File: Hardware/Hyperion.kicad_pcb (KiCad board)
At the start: 2 copper layers, 90.2 x 95.9 mm, 1 part

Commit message: Rough USB interface
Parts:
- added D1: TVS, CAPC1005-N, F.Cu at (182.0, 126.5)
- added D2: TVS, CAPC1005-N, F.Cu at (182.0, 124.2)
- added J1: CONN-DC, CONN-DC-CUI-202, F.Cu at (191.0, 112.0)
- added J2: USB, CONN-USB-MICRO-B-FCI, F.Cu at (190.0, 125.0)
- added R1: MOV, RESC1005-N, F.Cu at (184.0, 127.0)
- added R2: MOV, RESC1005-N, F.Cu at (184.0, 123.0)
- added TH1: PTC, RESC1005-N, F.Cu at (183.0, 129.5)
- added U1: FT2232H, QFP50P1200X1200-64N, F.Cu at (169.8, 124.8)
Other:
- net class Default: clearance 0.254 -> 0.2032; trace_width 0.254 -> 0.2032
- rule trace_clearance: 0.254 -> 0.2032
- rule trace_min: 0.254 -> 0.1524

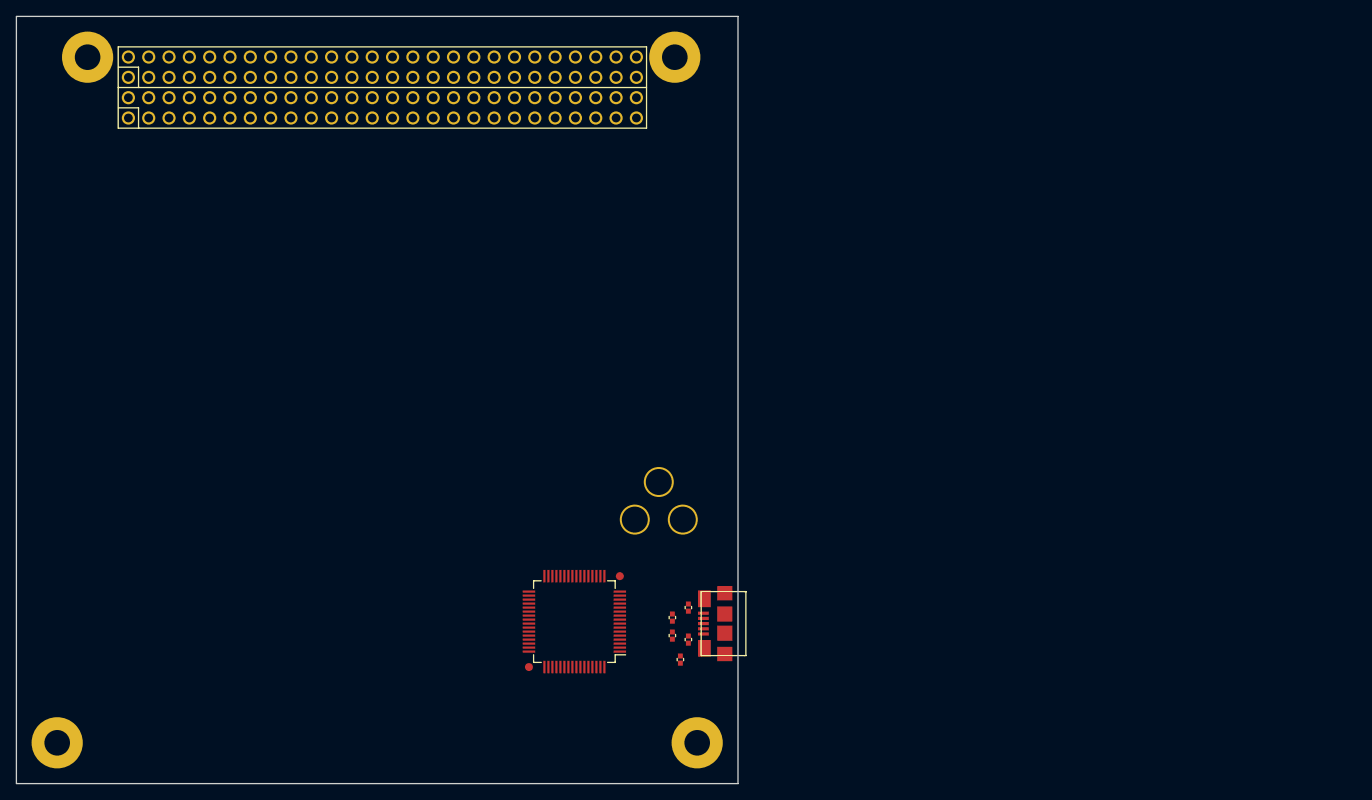
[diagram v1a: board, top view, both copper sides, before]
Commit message: Add protection circuit to DC jack
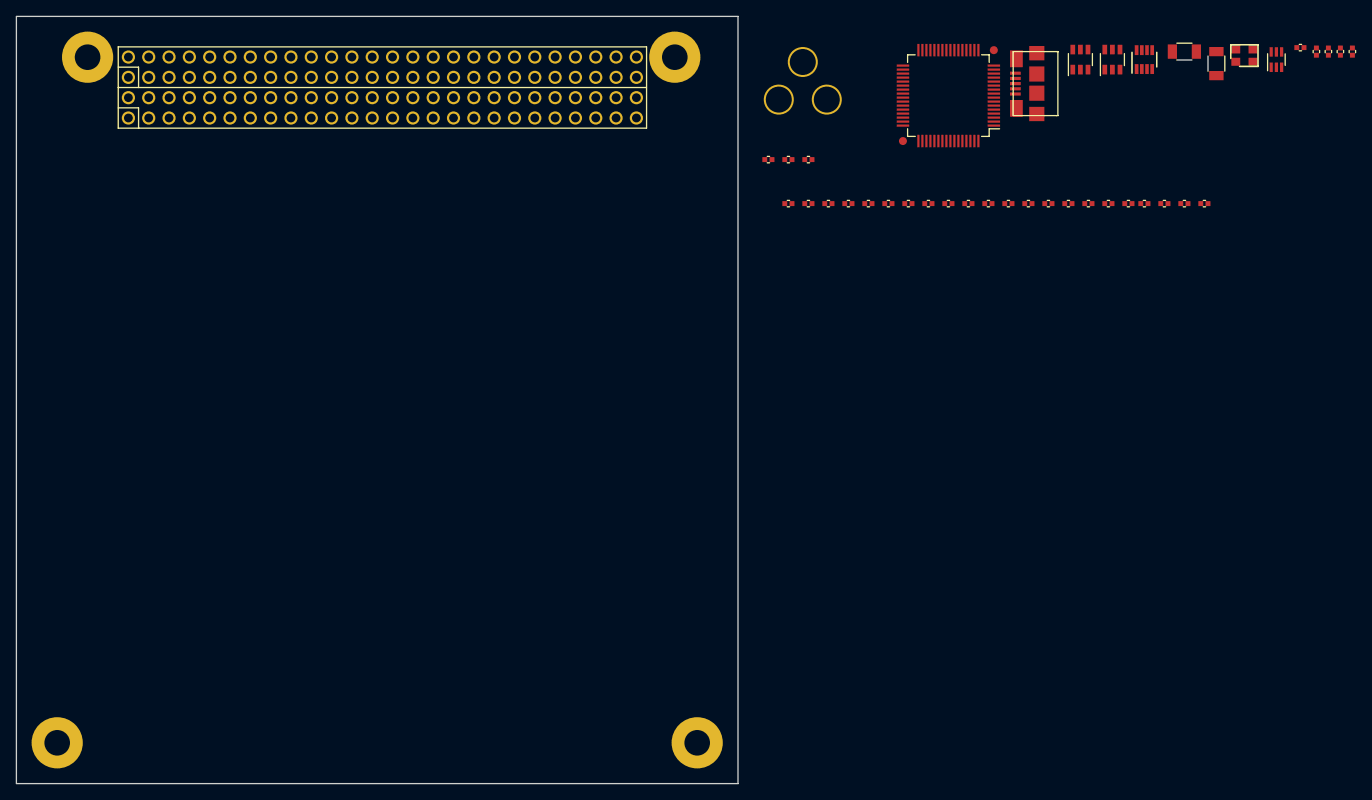
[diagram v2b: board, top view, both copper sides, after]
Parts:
- added C1: 3.3uF, CAPC1005-N, F.Cu at (229.0, 72.5)
- added C10: 0.1uF, CAPC1005-N, F.Cu at (199.0, 72.5)
- added C11: 27pF, CAPC1005-N, F.Cu at (234.0, 72.5)
- added C12: 0.1uF, CAPC1005-N, F.Cu at (216.5, 72.5)
- added C13: 0.1uF, CAPC1005-N, F.Cu at (236.5, 72.5)
- added C14: 27pF, CAPC1005-N, F.Cu at (231.5, 72.5)
- added C15: 0.1uF, CAPC1005-N, F.Cu at (224.0, 72.5)
- added C16: 0.1uF, CAPC1005-N, F.Cu at (260.5, 53.0)
- added C2: 0.1uF, CAPC1005-N, F.Cu at (214.0, 72.5)
- added C3: 3.3uF, CAPC1005-N, F.Cu at (226.5, 72.5)
- added C4: 0.1uF, CAPC1005-N, F.Cu at (211.5, 72.5)
- added C5: 0.1uF, CAPC1005-N, F.Cu at (209.0, 72.5)
- added C6: 3.3uF, CAPC1005-N, F.Cu at (221.5, 72.5)
- added C7: 0.1uF, CAPC1005-N, F.Cu at (206.5, 72.5)
- added C8: 0.1uF, CAPC1005-N, F.Cu at (204.0, 72.5)
- added C9: 0.1uF, CAPC1005-N, F.Cu at (201.5, 72.5)
- added FB1: 600, INDC1005-N, F.Cu at (241.0, 72.5)
- added FB2: 600, INDC1005-N, F.Cu at (239.0, 72.5)
- added Q1: MOSFET-P, SOT65P210-DDGSDD-N, F.Cu at (257.5, 54.5)
- added Q2: FDC6561, SOT95P280-6N, F.Cu at (233.0, 54.5)
- added R10: 10k, RESC1005-N, F.Cu at (199.0, 67.0)
- added R11: 0.02, RESC3216-N, F.Cu at (246.0, 53.5)
- added R3: 12k, RESC1005-N, F.Cu at (196.5, 72.5)
- added R4: 10k, RESC1005-N, F.Cu at (246.0, 72.5)
- added R5: 10k, RESC1005-N, F.Cu at (194.0, 67.0)
- added R6: 10k, RESC1005-N, F.Cu at (219.0, 72.5)
- added R7: 2.2k, RESC1005-N, F.Cu at (196.5, 67.0)
- added R8: 10k, RESC1005-N, F.Cu at (243.5, 72.5)
- added R9: 10k, RESC1005-N, F.Cu at (248.5, 72.5)
- added U2: 93LC46/OT, SOT95P280-6N, F.Cu at (237.0, 54.5)
- added U3: LTC4361-T, SOT65P280-8N, F.Cu at (241.0, 54.5)
- added X1: 12MHz, XTAL-4SMD-32X25, F.Cu at (253.5, 54.0)
- J1: value CONN-DC -> USB; footprint CONN-DC-CUI-202 -> CONN-USB-MICRO-B-FCI
- J2: value USB -> CONN-DC; footprint CONN-USB-MICRO-B-FCI -> CONN-DC-CUI-202
- TH1: footprint RESC1005-N -> RESC3216-N
- moved D1 110.9 mm to (265.5, 53.5)
- moved D2 110.6 mm to (267.0, 53.5)
- moved R1 107.5 mm to (262.5, 53.5)
- moved R2 106.0 mm to (264.0, 53.5)
- moved TH1 100.2 mm to (250.0, 55.0)
- moved U1 80.7 mm to (216.5, 59.0)
- moved J2 68.2 mm to (209.0, 59.5), turned to 270 degrees
- moved J1 66.4 mm to (229.0, 57.5), turned to 90 degrees
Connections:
- net +5V renamed +5VP
- H1 pad 1.32: (no net) -> VCOM
- H1 pad 2.27: +3.3V -> +3.3VP
- H1 pad 2.28: +3.3V -> +3.3VP
- J1 pad 1: (no net) -> N-00000102
- J1 pad 2: (no net) -> /Interface Port/D-
- J1 pad 3: (no net) -> /Interface Port/D+
- J2 pad 1: N-0000054 -> N-0000091
- J2 pad 2: /Interface Port/D- -> (no net)
- J2 pad 3: /Interface Port/D+ -> (no net)
- R1 pad 2: N-0000054 -> N-00000102
- R2 pad 2: N-0000055 -> GND
- TH1 pad 1: (no net) -> VCOM
- TH1 pad 2: N-0000054 -> N-00000102
- U1 pad 1: (no net) -> GND
- U1 pad 10: (no net) -> GND
- U1 pad 11: (no net) -> GND
- U1 pad 12: (no net) -> +1.8V
- U1 pad 13: (no net) -> GND
- U1 pad 14: (no net) -> /Interface Port/Reset
- U1 pad 15: (no net) -> GND
- U1 pad 2: (no net) -> /Interface Port/OSCI
- U1 pad 20: (no net) -> +3.3V
- U1 pad 25: (no net) -> GND
- U1 pad 3: (no net) -> /Interface Port/OSCO
- U1 pad 31: (no net) -> +3.3V
- U1 pad 35: (no net) -> GND
- U1 pad 37: (no net) -> +1.8V
- U1 pad 4: (no net) -> N-00000108
- U1 pad 42: (no net) -> +3.3V
- U1 pad 47: (no net) -> GND
- U1 pad 49: (no net) -> +1.8V
- U1 pad 5: (no net) -> GND
- U1 pad 50: (no net) -> +3.3V
- U1 pad 51: (no net) -> GND
- U1 pad 56: (no net) -> +3.3V
- U1 pad 59: (no net) -> /Interface Port/PwrSav
- U1 pad 6: (no net) -> N-00000101
- U1 pad 61: (no net) -> /Interface Port/DAT
- U1 pad 62: (no net) -> /Interface Port/CLK
- U1 pad 63: (no net) -> /Interface Port/CS
- U1 pad 64: (no net) -> +1.8V
- U1 pad 9: (no net) -> N-00000109

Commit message: Core support circuitry
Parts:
- added C17: 0.1uF, CAPC1005-N, F.Cu at (145.5, 79.0)
- added C18: 0.1uF, CAPC1005-N, F.Cu at (136.0, 79.0)
- added C19: 0.1uF, CAPC1005-N, F.Cu at (133.5, 79.0)
- added C20: 0.1uF, CAPC1005-N, F.Cu at (126.0, 86.5)
- added C21: 0.1uF, CAPC1005-N, F.Cu at (126.0, 93.0)
- added C22: 0.1uF, CAPC1005-N, F.Cu at (126.0, 98.0)
- added C23: 0.1uF, CAPC1005-N, F.Cu at (134.5, 106.5)
- added C24: 0.1uF, CAPC1005-N, F.Cu at (144.0, 110.0)
- added C25: 0.1uF, CAPC1005-N, F.Cu at (144.5, 105.0)
- added C26: 0.1uF, CAPC1005-N, F.Cu at (152.0, 98.5)
- added C27: 0.1uF, CAPC1005-N, F.Cu at (152.0, 93.0)
- added C28: 0.1uF, CAPC1005-N, F.Cu at (152.0, 86.5)
- added C29: 3.3uF, CAPC1005-N, F.Cu at (150.0, 81.0)
- added C30: 3.3uF, CAPC1005-N, F.Cu at (128.0, 103.0)
- added C31: 0.1uF, CAPC1005-N, F.Cu at (126.0, 89.5)
- added C32: 3.3uF, CAPC1005-N, F.Cu at (153.5, 93.0)
- added C33: 10pF, CAPC1005-N, F.Cu at (139.0, 105.0)
- added C34: 10pF, CAPC1005-N, F.Cu at (130.2, 105.0)
- added C35: 10pF, CAPC1005-N, F.Cu at (141.0, 105.0)
- added C36: 10pF, CAPC1005-N, F.Cu at (132.2, 105.0)
- added C37: 0.1uF, CAPC1005-N, F.Cu at (143.5, 79.0)
- added C38: 0.1uF, CAPC1005-N, F.Cu at (134.5, 105.0)
- added C39: 0.1uF, CAPC1005-N, F.Cu at (137.0, 105.0)
- added FB3: FERRITE, INDC1005-N, F.Cu at (143.5, 77.5)
- added R12: 1k, RESC1005-N, F.Cu at (137.0, 106.5)
- added U4: TM4C123GH6PGE, QFP50P2200X2200-144N, F.Cu at (139.0, 92.0)
- added X2: 12MHz, XTAL-4SMD-32X25, F.Cu at (140.0, 107.5)
- added X3: 32.768kHz, XTAL-2SMD-32x15, F.Cu at (131.2, 107.0)
- C11, C14: value 27pF -> 10pF
- moved C16 145.7 mm to (136.5, 129.5)
- moved D1 145.7 mm to (141.5, 130.0)
- moved D2 145.7 mm to (143.0, 130.0)
- moved Q1 145.7 mm to (133.5, 131.0)
- moved Q2 145.7 mm to (109.0, 131.0)
- moved R1 145.7 mm to (138.5, 130.0)
- moved R11 145.7 mm to (122.0, 130.0)
- moved R2 145.7 mm to (140.0, 130.0)
- moved TH1 145.7 mm to (126.0, 131.5)
- moved U2 145.7 mm to (113.0, 131.0)
- moved U3 145.7 mm to (117.0, 131.0)
- moved X1 145.7 mm to (129.5, 130.5)
- moved C1 105.5 mm to (139.0, 127.5)
- moved C10 105.5 mm to (109.0, 127.5)
- moved C11 105.5 mm to (144.0, 127.5)
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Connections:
- H1 pad 1.42: (no net) -> VMEM
- U1 pad 16: (no net) -> /Core/TCK
- U1 pad 17: (no net) -> /Core/TDI
- U1 pad 18: (no net) -> /Core/TDO
- U1 pad 19: (no net) -> /Core/TMS
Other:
- copper layers 2 -> 4
- net class Default: clearance 0.2032 -> 0.1524; trace_width 0.2032 -> 0.1524; via_dia 0.889 -> 0.4572; via_drill 0.635 -> 0.254
- rule trace_clearance: 0.2032 -> 0.1524
- rule trace_min: 0.1524 -> 0.127
- rule via_min_drill: 0.508 -> 0.254
- rule via_min_size: 0.889 -> 0.4572

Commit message: Rough layout
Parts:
- moved R3 70.5 mm to (176.2, 117.0), turned to 180 degrees
- moved R5 60.8 mm to (164.8, 123.5), turned to 270 degrees
- moved TH1 58.4 mm to (182.0, 114.8), turned to 270 degrees
- moved R7 56.4 mm to (162.8, 125.8), turned to 270 degrees
- moved R10 54.1 mm to (162.8, 128.2), turned to 270 degrees
- moved C10 53.2 mm to (162.0, 123.5), turned to 270 degrees
- moved C7 52.9 mm to (165.0, 106.5), turned to 90 degrees
- moved U2 52.7 mm to (165.5, 127.0), turned to 180 degrees
- moved Q2 52.2 mm to (161.0, 136.0), turned to 90 degrees
- moved C4 50.8 mm to (171.2, 117.0)
- moved C8 50.1 mm to (159.5, 106.5), turned to 90 degrees
- moved C2 49.1 mm to (171.2, 114.0)
- moved U3 48.5 mm to (165.2, 136.0), turned to 180 degrees
- moved R1 47.5 mm to (184.0, 116.5)
- moved R2 47.4 mm to (184.0, 112.5)
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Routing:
- net /Interface Port/D+: track 0.00 -> 18.0 mm
- net /Interface Port/D-: track 0.00 -> 17.9 mm
- net /Interface Port/OSCI: track 0.00 -> 9.80 mm
- net N-00000109: track 0.00 -> 9.72 mm
- net N-00000108: track 0.00 -> 9.62 mm
- net /Interface Port/OSCO: track 0.00 -> 8.67 mm
- net N-00000101: track 0.00 -> 8.36 mm
- net GND: track 0.00 -> 7.30 mm, vias 0 -> 4
- net N-00000105: track 0.00 -> 4.09 mm
- added copper zone on F.Cu, net /Interface Port/Shield
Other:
- net class USB added: clearance 0.2032, trace_width 0.254, via_dia 0.4572, via_drill 0.254

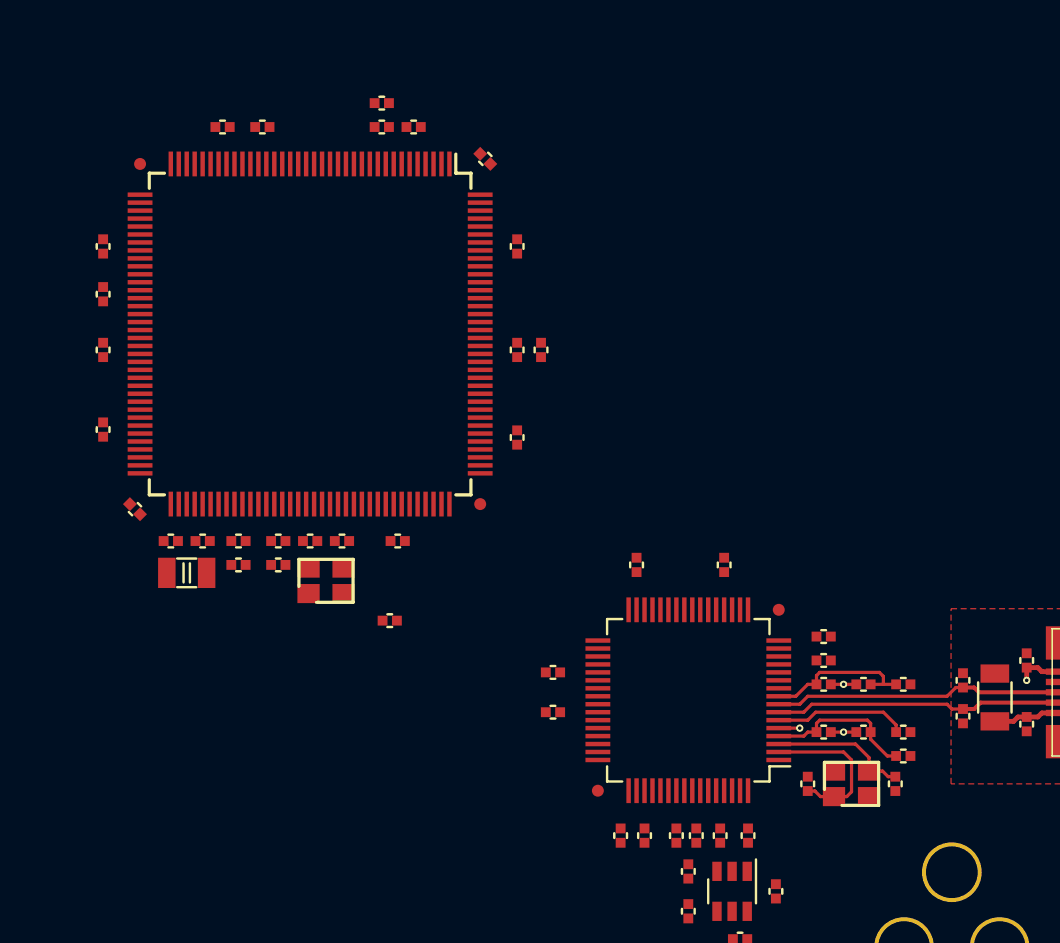
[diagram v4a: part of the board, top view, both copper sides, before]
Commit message: Testing bottom side decoupling
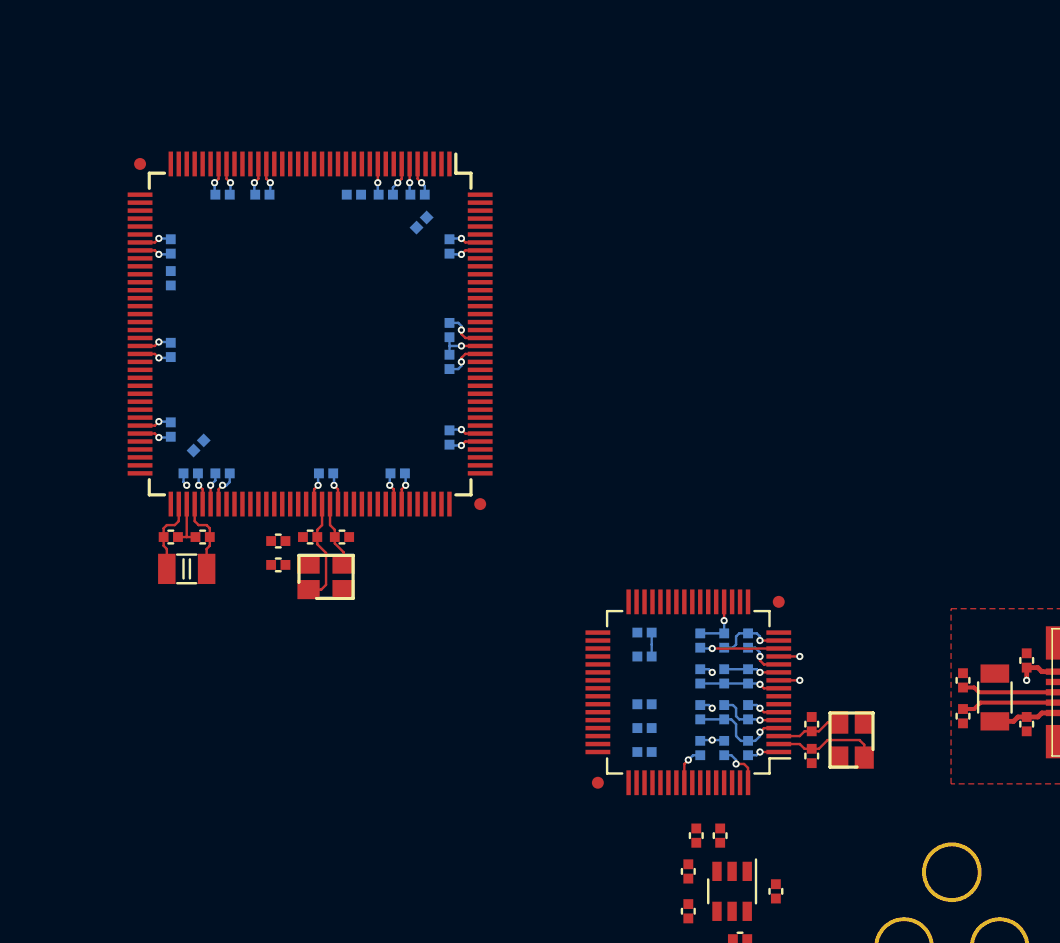
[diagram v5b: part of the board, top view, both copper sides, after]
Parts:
- C1, C10, C12, C13, C16, C17, C18, C19, C2, C20, C21, C22, C23, C24, C25, C26, C27, C28, C29, C3, C30, C31, C32, C37, C38, C4, C5, C6, C7, C8, C9, FB1, FB2, FB3, R3, R9: moved to B.Cu
- moved FB2 13.0 mm to (163.5, 115.8), turned to 90 degrees
- moved FB1 12.8 mm to (163.5, 113.5), turned to 90 degrees
- moved C24 10.1 mm to (140.0, 100.8)
- moved R3 9.83 mm to (166.5, 115.8), turned to 90 degrees
- moved C3 8.84 mm to (165.0, 115.8), turned to 90 degrees
- moved C1 8.76 mm to (165.0, 113.5), turned to 90 degrees
- moved R9 7.75 mm to (163.5, 111.2), turned to 90 degrees
- moved C6 6.91 mm to (160.0, 116.8), turned to 0 degrees
- moved C14 6.45 mm to (170.5, 116.5), turned to 90 degrees
- moved FB3 6.01 mm to (141.8, 83.2), turned to 180 degrees
- moved C32 5.88 mm to (147.8, 91.8)
- moved C13 5.84 mm to (160.0, 112.2), turned to 0 degrees
- moved C23 5.84 mm to (133.5, 100.8)
- moved C9 5.77 mm to (160.0, 115.2), turned to 0 degrees
- moved C10 5.70 mm to (163.5, 118.0), turned to 90 degrees
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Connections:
- H1 pad 2.17: (no net) -> /Core/ADCS0
- H1 pad 2.18: (no net) -> /Core/ADCS1
- H1 pad 2.19: (no net) -> /Core/ADCS2
- H1 pad 2.20: (no net) -> /Core/ADCS3
- H1 pad 2.21: (no net) -> /Core/ADCS4
- H1 pad 2.22: (no net) -> /Core/ADCS5
- H1 pad 2.23: (no net) -> /Core/ADCS6
- H1 pad 2.24: (no net) -> /Core/ADCS7
- U4 pad 21: (no net) -> /Core/ADCS7
- U4 pad 22: (no net) -> /Core/ADCS6
- U4 pad 23: (no net) -> /Core/ADCS5
- U4 pad 26: (no net) -> /Core/ADCS4
- U4 pad 27: (no net) -> /Core/ADCS3
- U4 pad 28: (no net) -> /Core/ADCS2
- U4 pad 31: (no net) -> /Core/ADCS1
- U4 pad 32: (no net) -> /Core/ADCS0
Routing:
- net GND: track 7.30 -> 51.2 mm, vias 4 -> 22
- net +3.3V: track 0.00 -> 32.8 mm, vias 0 -> 16
- net /Interface Port/D+: track 18.0 -> 6.00 mm
- net /Interface Port/D-: track 17.9 -> 6.04 mm
- net /Core/OSC0: track 0.00 -> 6.65 mm
- net N-00000102: track 8.36 -> 2.12 mm, vias 0 -> 1
- net +1.8V: track 0.00 -> 5.57 mm, vias 0 -> 2
- net /Interface Port/Reset: track 0.00 -> 4.95 mm, vias 0 -> 1
- net /Core/XOSC1: track 0.00 -> 4.84 mm
- net /Core/XOSC0: track 0.00 -> 4.84 mm
- net N-00000110: track 9.72 -> 5.05 mm, vias 0 -> 1
- net /Interface Port/OSCO: track 8.67 -> 4.12 mm
- net /Core/OSC1: track 0.00 -> 4.12 mm
- net N-00000109: track 9.62 -> 6.41 mm, vias 0 -> 1
- net /Core/GNDX: track 0.00 -> 3.17 mm
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- added copper zone on Inner1.Cu, net GND
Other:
- net class USB removed

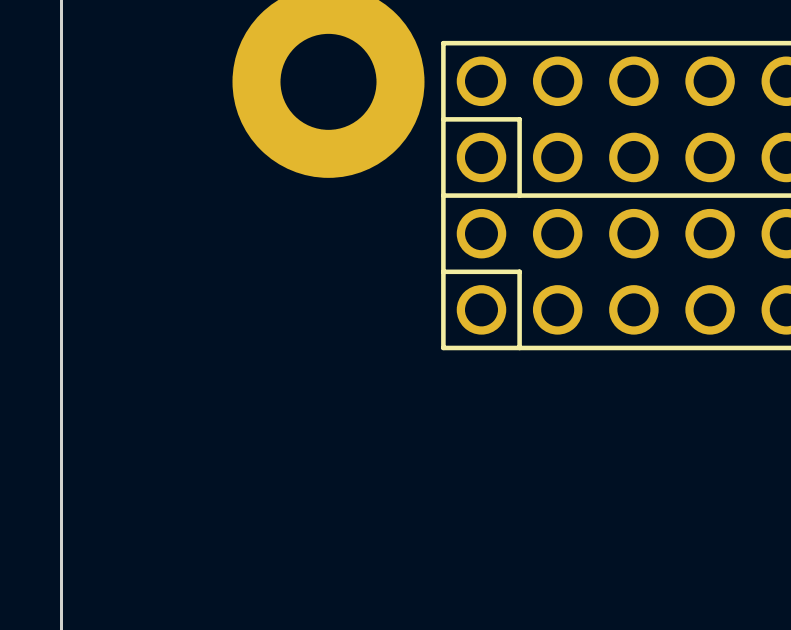
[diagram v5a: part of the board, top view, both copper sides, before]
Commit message: Add CAN transceiver
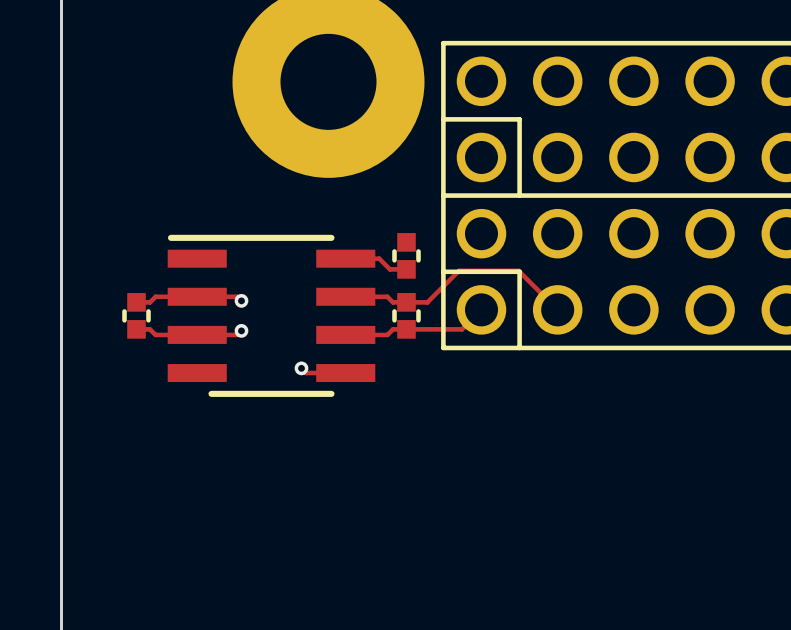
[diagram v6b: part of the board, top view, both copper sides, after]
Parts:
- added C40: 0.1uF, CAPC1005-N, F.Cu at (102.5, 62.0)
- added R13: 10k, RESC1005-N, F.Cu at (111.5, 60.0)
- added R14: 120, RESC1005-N, F.Cu at (111.5, 62.0)
- added U5: SN65HVD233, SOIC127P600-8N, F.Cu at (107.0, 62.0)
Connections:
- H1 pad 1.1: (no net) -> /Core/CANL
- H1 pad 1.3: (no net) -> /Core/CANH
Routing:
- net /Core/CANH: track 0.00 -> 8.12 mm
- net GND: track 51.2 -> 56.3 mm, vias 22 -> 24
- net /Core/CANL: track 0.00 -> 4.87 mm
- net +3.3V: track 32.8 -> 36.5 mm, vias 16 -> 17
- net N-00000120: track 0.00 -> 2.17 mm
